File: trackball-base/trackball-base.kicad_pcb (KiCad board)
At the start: 2 copper layers, 110 x 140 mm, 155 parts, among them J201 TYPE-C-31-M-12, J202 CORTEX-DBG-10, Q101 2N7002, SW201 RESET, SW202 BOOT, SW401 D2FC-F-7N, SW402 D2FC-F-7N, SW403 D2FC-F-7N, U101 AP2112K-3.3TRG1, U102 APX809-29SAG-7, U103 XC6206P192MR, U104 TPS22918DBVR, U105 TPS22918DBVR, U106 TLV3011AIDBVR, U107 TLV3011AIDBVR, U201 E73-2G4M08S1C, U202 TPD2E1B06DRLR, U301 PMW3360DM-T2QU, U302 PMW3360DM-T2QU, U501 LTC4125EUFD, Y201 ABS07-32.768KHZ-9-T

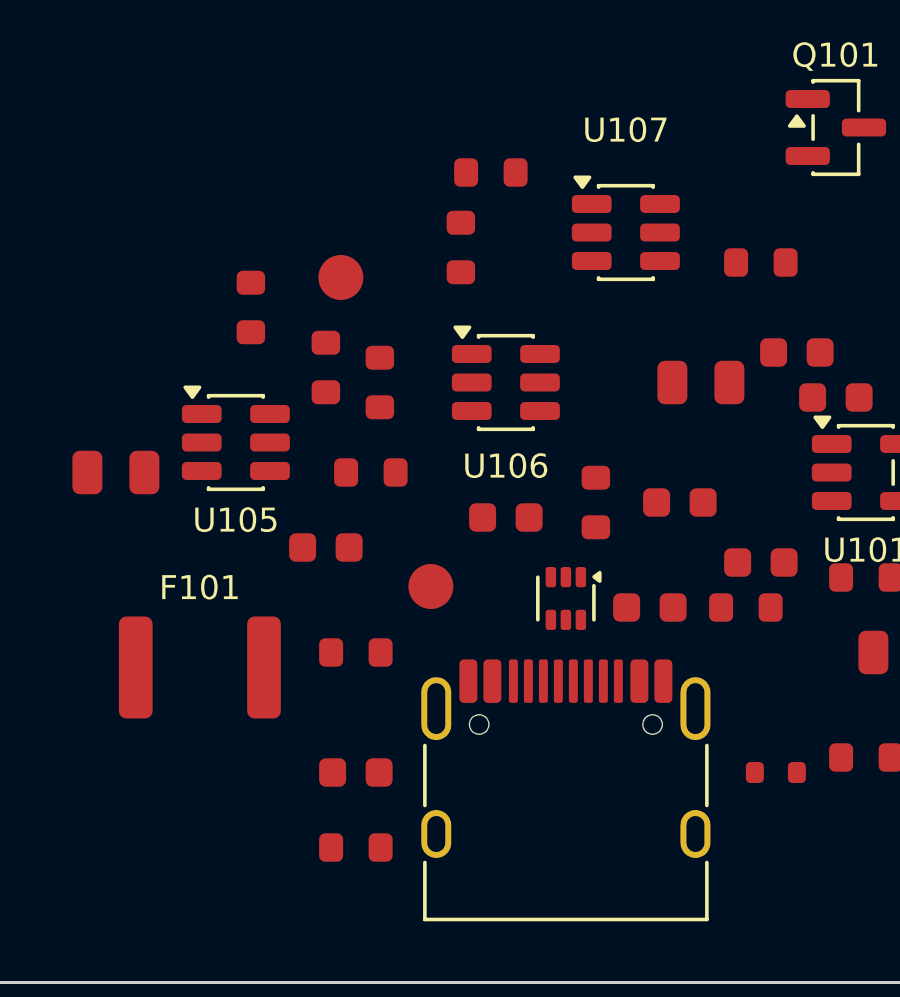
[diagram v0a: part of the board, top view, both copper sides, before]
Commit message: layout: USB-fanout placement ECO (drc17: 0 errors/0 parity)
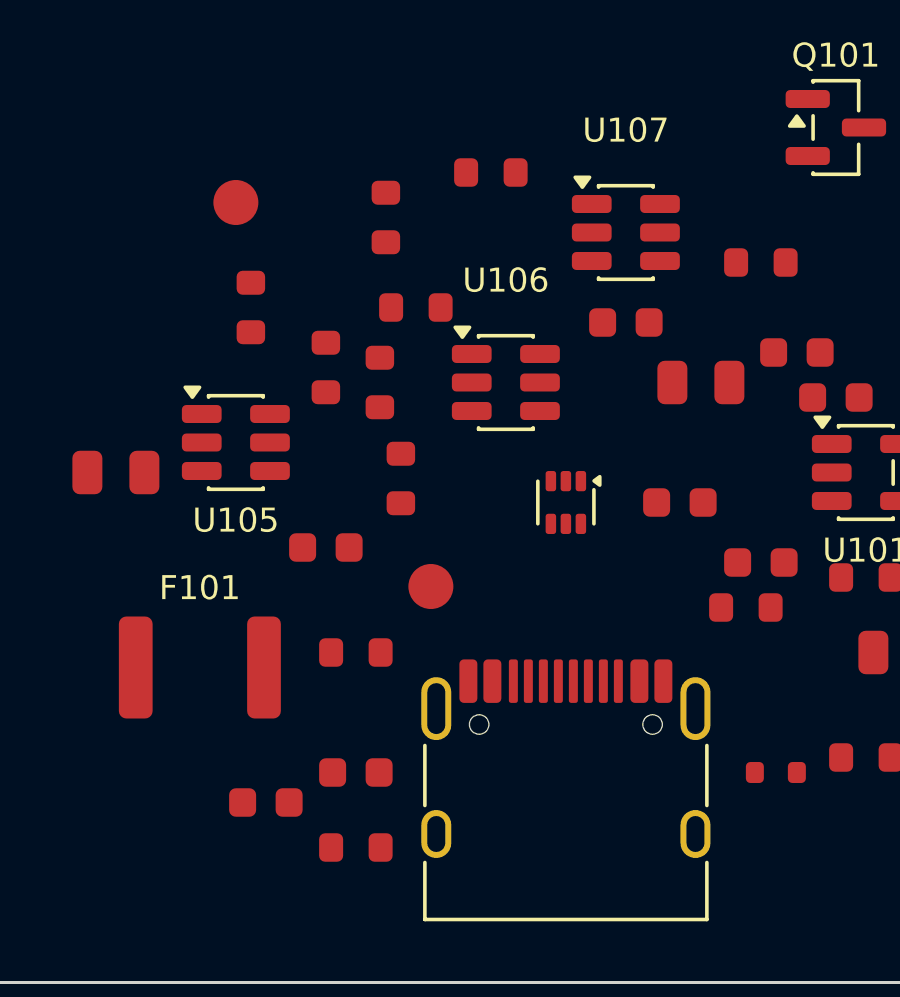
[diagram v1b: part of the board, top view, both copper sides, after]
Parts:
- moved C102 14.4 mm to (45.0, 134.0)
- moved C115 7.63 mm to (57.0, 118.0)
- moved R104 6.55 mm to (49.5, 123.2)
- moved R105 5.70 mm to (50.0, 117.5)
- moved TP105 4.30 mm to (44.0, 114.0)
- moved U202 3.20 mm to (55.0, 124.0)
- moved R107 2.69 mm to (49.0, 114.5)

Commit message: WIP routing drc143: unc 57, 0 viol, VBUS12/GND11
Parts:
- moved TP308 32.0 mm to (44.0, 54.0)
- moved TP202 31.0 mm to (33.0, 40.0)
- moved TP304 26.0 mm to (30.0, 54.0)
- moved TP307 26.0 mm to (44.0, 50.0)
- moved TP302 23.2 mm to (30.0, 46.0)
- moved TP303 19.9 mm to (30.0, 50.0)
- moved TP306 18.8 mm to (44.0, 46.0)
- moved TP301 17.6 mm to (30.0, 42.0)
- moved TP204 17.2 mm to (10.8, 14.0)
- moved C115 14.9 mm to (46.0, 108.0)
- moved TP305 14.1 mm to (44.0, 42.0)
- moved R514 13.2 mm to (79.0, 9.00)
- moved TP501 12.9 mm to (80.0, 12.0)
- moved R203 12.0 mm to (40.0, 120.0)
- moved R513 10.2 mm to (65.0, 28.0)
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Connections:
- C111 pad 2: (no net) -> /power/Net-(U104-CT)
- C116 pad 2: (no net) -> /power/Net-(U105-CT)
- C201 pad 2: (no net) -> /mcu/Net-(U201-P0.00/XL1)
- C202 pad 1: (no net) -> /mcu/Net-(U201-P0.01/XL2)
- C301 pad 2: (no net) -> /sensors/Net-(U301-VDDPIX)
- C302 pad 2: (no net) -> /sensors/Net-(U301-VDDPIX)
- C308 pad 2: (no net) -> /sensors/Net-(U302-VDDPIX)
- C309 pad 2: (no net) -> /sensors/Net-(U302-VDDPIX)
- C502 pad 2: (no net) -> /tx/Net-(U501-IS+)
- C507 pad 1: (no net) -> /tx/Net-(U501-CTD)
- C508 pad 1: (no net) -> /tx/Net-(U501-CTS)
- C509 pad 1: (no net) -> /tx/Net-(D501-A)
- C509 pad 2: (no net) -> /tx/Net-(U501-SW2)
- D501 pad 2: (no net) -> /tx/Net-(D501-A)
- J201 pad A5: (no net) -> /mcu/Net-(J201-CC1)
- J201 pad A6: (no net) -> /mcu/Net-(U202-IOB1)
- J201 pad A7: (no net) -> /mcu/Net-(U202-IOA1)
- J201 pad B5: (no net) -> /mcu/Net-(J201-CC2)
- J201 pad B6: (no net) -> /mcu/Net-(U202-IOB1)
- J201 pad B7: (no net) -> /mcu/Net-(U202-IOA1)
- J202 pad 2: (no net) -> /mcu/Net-(J202-Pin_2)
- J202 pad 4: (no net) -> /mcu/Net-(J202-Pin_4)
- L501 pad 2: (no net) -> /tx/Net-(D501-A)
- Q101 pad 1: (no net) -> /power/Net-(Q101-G)
- R104 pad 2: (no net) -> /power/Net-(U106-IN+)
- R105 pad 1: (no net) -> /power/Net-(U106-IN+)
- R106 pad 1: (no net) -> /power/Net-(U106-IN+)
- R107 pad 2: (no net) -> /power/Net-(U107-IN+)
- R108 pad 1: (no net) -> /power/Net-(U107-IN+)
- R109 pad 1: (no net) -> /power/Net-(U107-IN+)
- R109 pad 2: (no net) -> /power/Net-(Q101-G)
- R110 pad 2: (no net) -> /power/Net-(Q101-G)
- R201 pad 2: (no net) -> /mcu/Net-(U201-P1.11)
- R203 pad 2: (no net) -> /mcu/Net-(J201-CC1)
- R204 pad 1: (no net) -> /mcu/Net-(J201-CC2)
- R206 pad 1: (no net) -> /mcu/Net-(U201-P0.13)
- R207 pad 2: (no net) -> /mcu/Net-(U201-P0.12)
- R302 pad 1: (no net) -> /sensors/Net-(U301-LED_P)
- R304 pad 1: (no net) -> /sensors/Net-(U302-LED_P)
- R401 pad 1: (no net) -> /buttons/Net-(SW401-NO)
- R403 pad 1: (no net) -> /buttons/Net-(SW402-NO)
- R405 pad 1: (no net) -> /buttons/Net-(SW403-NO)
- R502 pad 2: (no net) -> /tx/Net-(U501-IS+)
- R503 pad 2: (no net) -> /tx/Net-(U501-DTH)
- R504 pad 1: (no net) -> /tx/Net-(U501-DTH)
- R505 pad 2: (no net) -> /tx/Net-(U501-FTH)
- R506 pad 1: (no net) -> /tx/Net-(U501-FTH)
- R507 pad 2: (no net) -> /tx/Net-(U501-EN)
- R510 pad 2: (no net) -> /tx/Net-(U501-NTC)
- R514 pad 1: (no net) -> /tx/Net-(D501-A)
- R514 pad 2: (no net) -> /tx/Net-(R514-Pad2)
- SW202 pad 2: (no net) -> /mcu/Net-(U201-P1.11)
- SW401 pad 2: (no net) -> /buttons/Net-(SW401-NO)
- SW402 pad 2: (no net) -> /buttons/Net-(SW402-NO)
- SW403 pad 2: (no net) -> /buttons/Net-(SW403-NO)
- TH501 pad 1: (no net) -> /tx/Net-(U501-NTC)
- TP201 pad 1: (no net) -> /mcu/Net-(U201-P0.28/AIN4)
- TP202 pad 1: (no net) -> /mcu/Net-(U201-P0.29/AIN5)
- TP203 pad 1: (no net) -> /mcu/Net-(J202-Pin_2)
- TP204 pad 1: (no net) -> /mcu/Net-(J202-Pin_4)
- TP501 pad 1: (no net) -> /tx/Net-(R514-Pad2)
- U104 pad 4: (no net) -> /power/Net-(U104-CT)
- U105 pad 4: (no net) -> /power/Net-(U105-CT)
- U106 pad 3: (no net) -> /power/Net-(U106-IN+)
- U107 pad 1: (no net) -> /power/Net-(Q101-G)
- U107 pad 3: (no net) -> /power/Net-(U107-IN+)
- U201 pad 1: (no net) -> /mcu/Net-(U201-P1.11)
- U201 pad 11: (no net) -> /mcu/Net-(U201-P0.00/XL1)
- U201 pad 13: (no net) -> /mcu/Net-(U201-P0.01/XL2)
- U201 pad 20: (no net) -> /mcu/Net-(U201-P0.12)
- U201 pad 29: (no net) -> /mcu/Net-(U201-D-)
- U201 pad 31: (no net) -> /mcu/Net-(U201-D+)
- U201 pad 33: (no net) -> /mcu/Net-(U201-P0.13)
- U201 pad 37: (no net) -> /mcu/Net-(J202-Pin_2)
- U201 pad 39: (no net) -> /mcu/Net-(J202-Pin_4)
- U201 pad 4: (no net) -> /mcu/Net-(U201-P0.28/AIN4)
- U201 pad 8: (no net) -> /mcu/Net-(U201-P0.29/AIN5)
- U202 pad 1: (no net) -> /mcu/Net-(U202-IOA1)
- U202 pad 2: (no net) -> /mcu/Net-(U202-IOB1)
- U202 pad 4: (no net) -> /mcu/Net-(U201-D+)
- U202 pad 5: (no net) -> /mcu/Net-(U201-D-)
- U301 pad 15: (no net) -> /sensors/Net-(U301-LED_P)
- U301 pad 3: (no net) -> /sensors/Net-(U301-VDDPIX)
- U302 pad 15: (no net) -> /sensors/Net-(U302-LED_P)
- U302 pad 3: (no net) -> /sensors/Net-(U302-VDDPIX)
- U501 pad 14: (no net) -> /tx/Net-(U501-CTD)
- U501 pad 15: (no net) -> /tx/Net-(U501-EN)
- U501 pad 18: (no net) -> /tx/Net-(U501-SW2)
- U501 pad 2: (no net) -> /tx/Net-(U501-CTS)
- U501 pad 4: (no net) -> /tx/Net-(U501-IS+)
- U501 pad 6: (no net) -> /tx/Net-(U501-NTC)
- U501 pad 7: (no net) -> /tx/Net-(U501-DTH)
- U501 pad 9: (no net) -> /tx/Net-(U501-FTH)
- Y201 pad 1: (no net) -> /mcu/Net-(U201-P0.01/XL2)
- Y201 pad 2: (no net) -> /mcu/Net-(U201-P0.00/XL1)
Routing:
- net GND: track 0.00 -> 1147.0 mm, vias 0 -> 31
- net +3V3: track 0.00 -> 326.9 mm, vias 0 -> 16
- net MCU_RST: track 0.00 -> 279.9 mm, vias 0 -> 15
- net BTN2: track 0.00 -> 166.2 mm, vias 0 -> 6
- net VIN: track 0.00 -> 164.7 mm, vias 0 -> 6
- net /mcu/Net-(U201-P1.11): track 0.00 -> 156.6 mm, vias 0 -> 6
- net /mcu/Net-(U201-D-): track 0.00 -> 144.4 mm, vias 0 -> 2
- net /mcu/Net-(U201-D+): track 0.00 -> 141.8 mm, vias 0 -> 2
- net S1_NCS: track 0.00 -> 140.7 mm, vias 0 -> 4
- net S1_MISO: track 0.00 -> 125.8 mm, vias 0 -> 2
- net TX_5V_SW: track 0.00 -> 125.1 mm, vias 0 -> 8
- net S2_SCK: track 0.00 -> 121.3 mm, vias 0 -> 4
- net S2_MISO: track 0.00 -> 118.2 mm, vias 0 -> 4
- net S2_NCS: track 0.00 -> 111.8 mm, vias 0 -> 5
- net VSEN_1V9: track 0.00 -> 109.8 mm, vias 0 -> 4
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
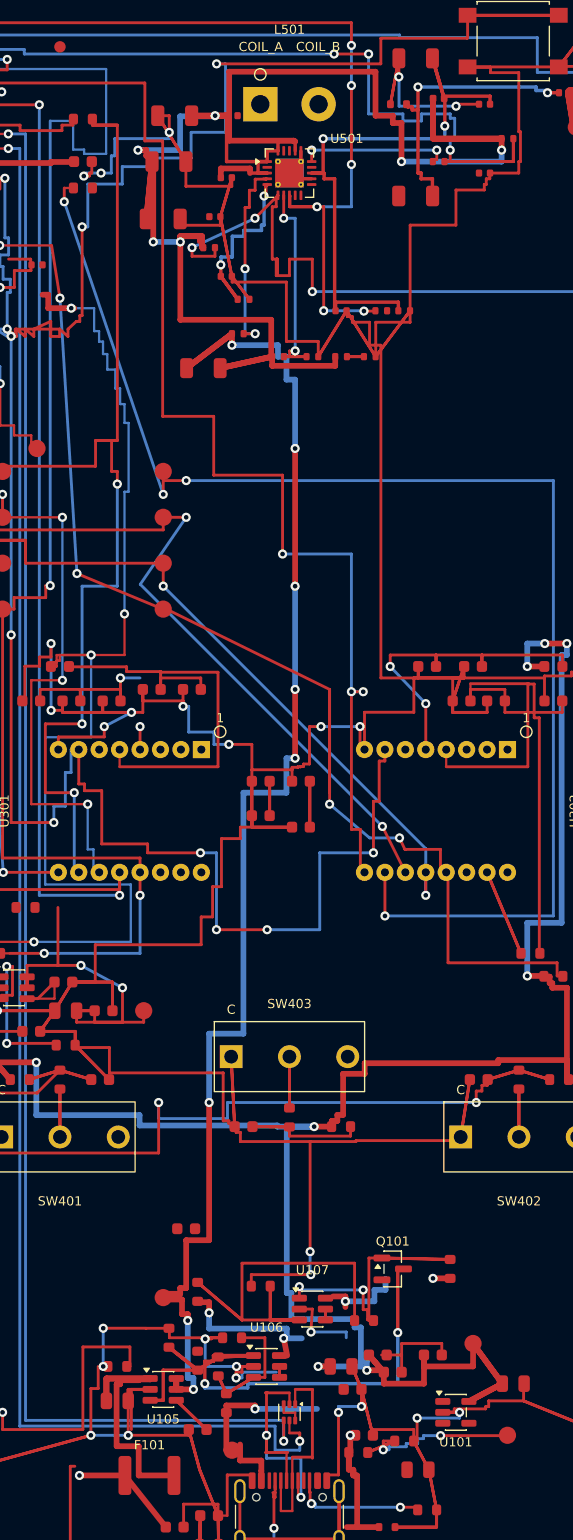
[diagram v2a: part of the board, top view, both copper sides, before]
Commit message: ECO batch1: C115 placed, U101 EN tied, R207/C509 spread, VIN/IS+ ripup (pre-freeroute unc64/0viol)
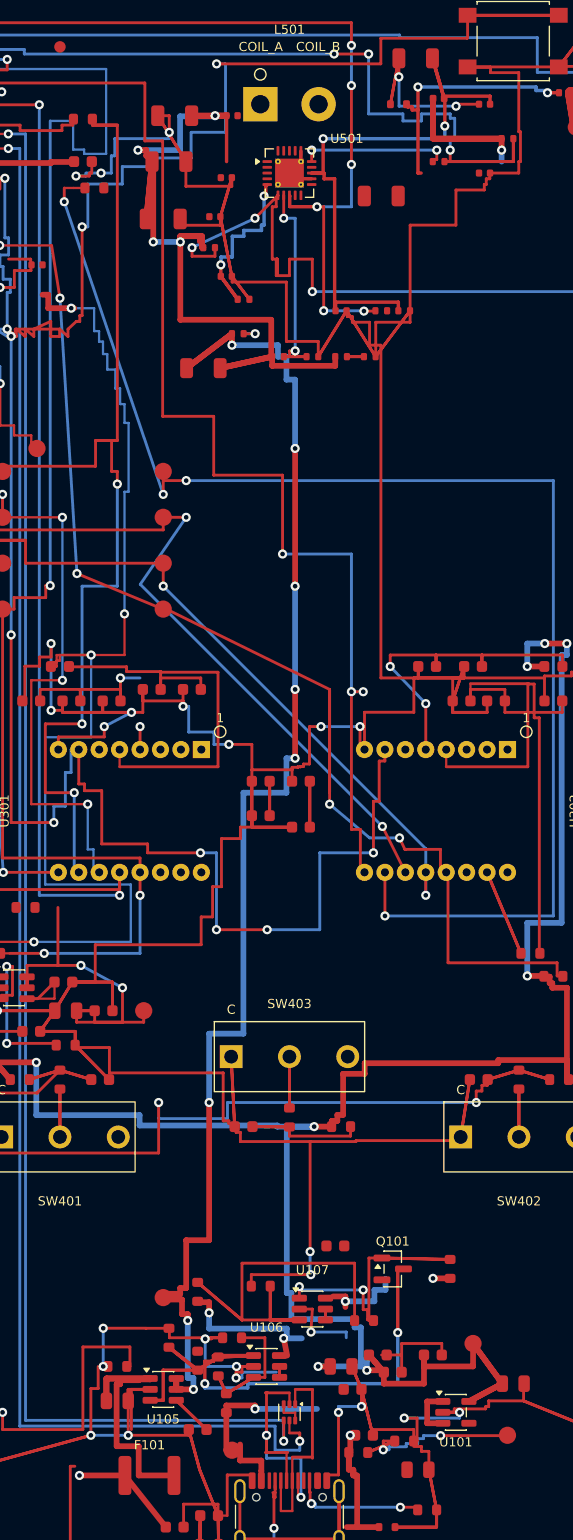
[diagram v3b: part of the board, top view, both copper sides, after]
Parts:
- moved C115 13.1 mm to (59.0, 109.5)
- moved C509 3.00 mm to (63.0, 18.0)
- moved R207 1.00 mm to (38.0, 17.3)
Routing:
- net VIN: track 164.7 -> 104.9 mm, vias 6 -> 5
- net /tx/Net-(U501-IS+): track 17.3 -> 1.88 mm, vias 2 -> 1
- net VBUS: track 70.0 -> 73.3 mm
- net /tx/Net-(D501-A): track 25.1 -> 22.1 mm
- net S2_SCK: track 121.3 -> 122.2 mm
- net GND: track 1147.0 -> 1147.5 mm

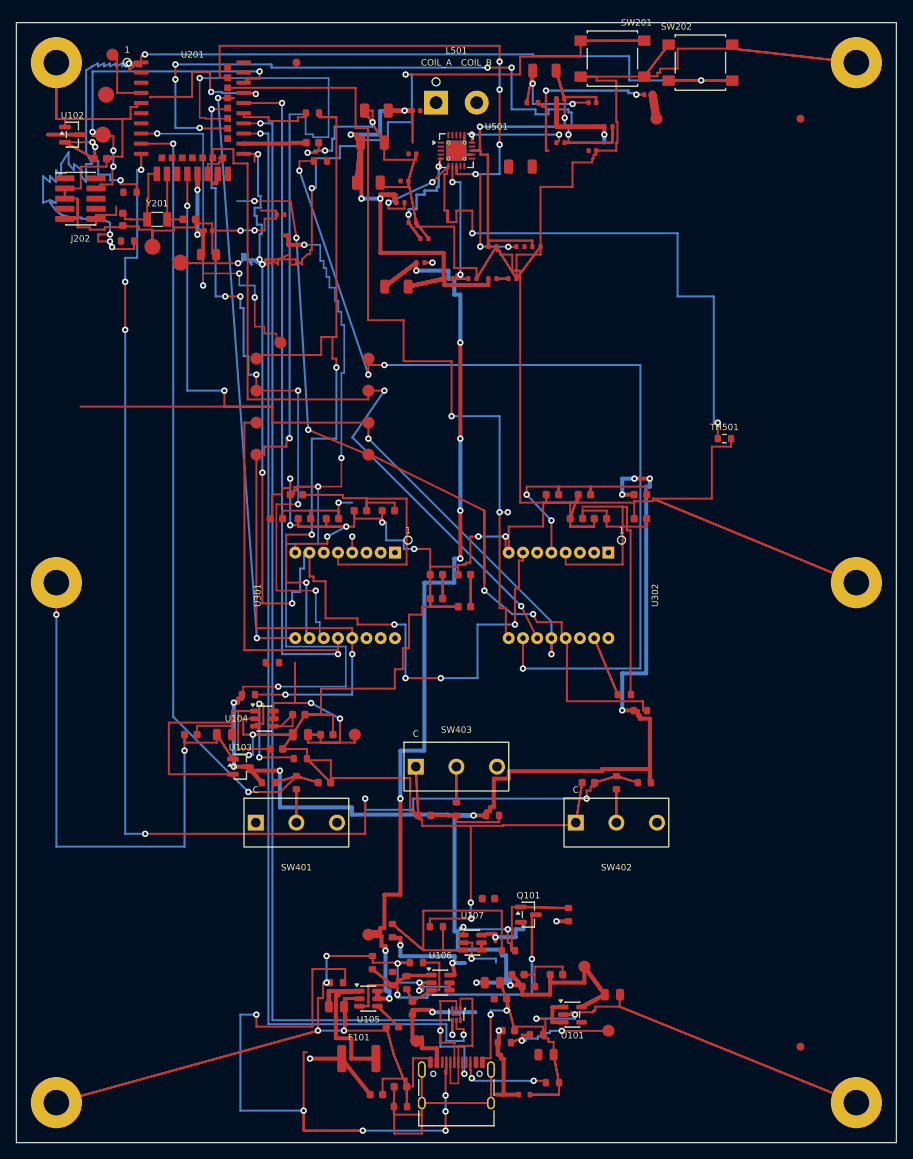
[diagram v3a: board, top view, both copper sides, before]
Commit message: layout: drc126 27unc/0err/0parity — BLOCKED Q5/Q6 (schematic-ECO 4 pads + placement decision)
Hand/survey P6-P130: 57->27 unconnected (-30), 0 errors, 0 parity.
Freerouting.org headless corroborates: stuck 73 unrouted, no progress.
QUESTIONS.md: Q5 (U501.14/U201.3/U201.42/U201.28 alt-taps) + Q6 (TP move + 23).
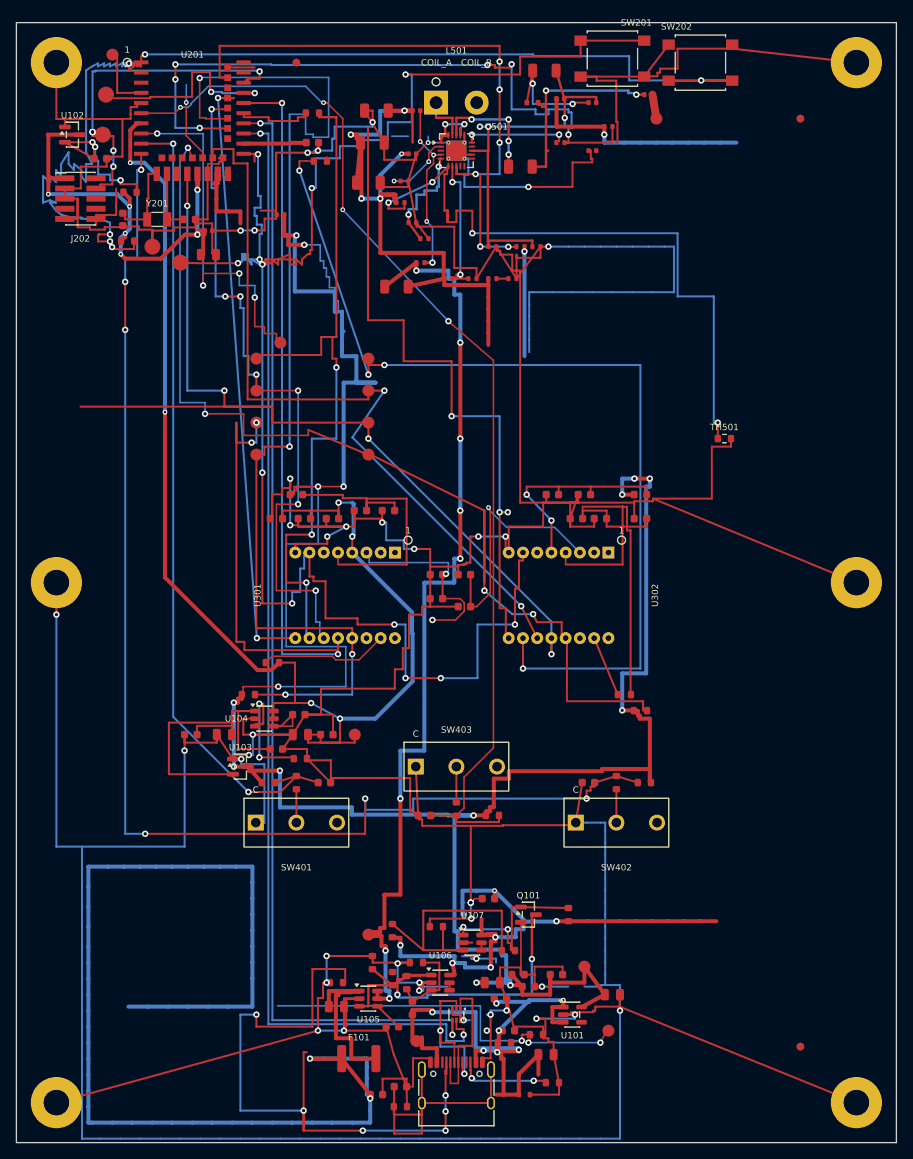
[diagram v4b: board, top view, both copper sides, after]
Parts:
- turned C507 to 180 degrees
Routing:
- net VBUS: track 73.3 -> 298.9 mm, vias 7 -> 15
- net BTN3: track 13.4 -> 136.2 mm, vias 0 -> 4
- net VSEN_1V9: track 109.8 -> 222.8 mm, vias 4 -> 6
- net +3V3: track 326.9 -> 405.7 mm, vias 16 -> 22
- net GND: track 1147.5 -> 1179.0 mm, vias 31 -> 40
- net VBUS_SENSE: track 19.0 -> 49.3 mm, vias 2 -> 3
- net /sensors/Net-(U302-VDDPIX): track 8.00 -> 31.8 mm, vias 0 -> 1
- net S2_MOT: track 106.1 -> 83.5 mm
- net /tx/Net-(U501-IS+): track 1.88 -> 23.2 mm, vias 1 -> 4
- net S2_NCS: track 111.8 -> 130.7 mm, vias 5 -> 4
- net /sensors/Net-(U301-VDDPIX): track 6.00 -> 24.7 mm, vias 0 -> 2
- net VIN: track 104.9 -> 122.2 mm, vias 5 -> 8
- net /sensors/Net-(U301-LED_P): track 0.00 -> 16.0 mm
- net /mcu/CHASSIS: track 53.9 -> 38.6 mm
- net /tx/Net-(U501-SW2): track 0.00 -> 14.8 mm, vias 0 -> 4
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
